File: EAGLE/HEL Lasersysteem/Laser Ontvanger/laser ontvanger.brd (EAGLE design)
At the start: 23 x 10 mm, 13 parts, among them IC1 HS0038A2, IC2 74LVC1G14DBV, IC3 74LVC1G14DBV

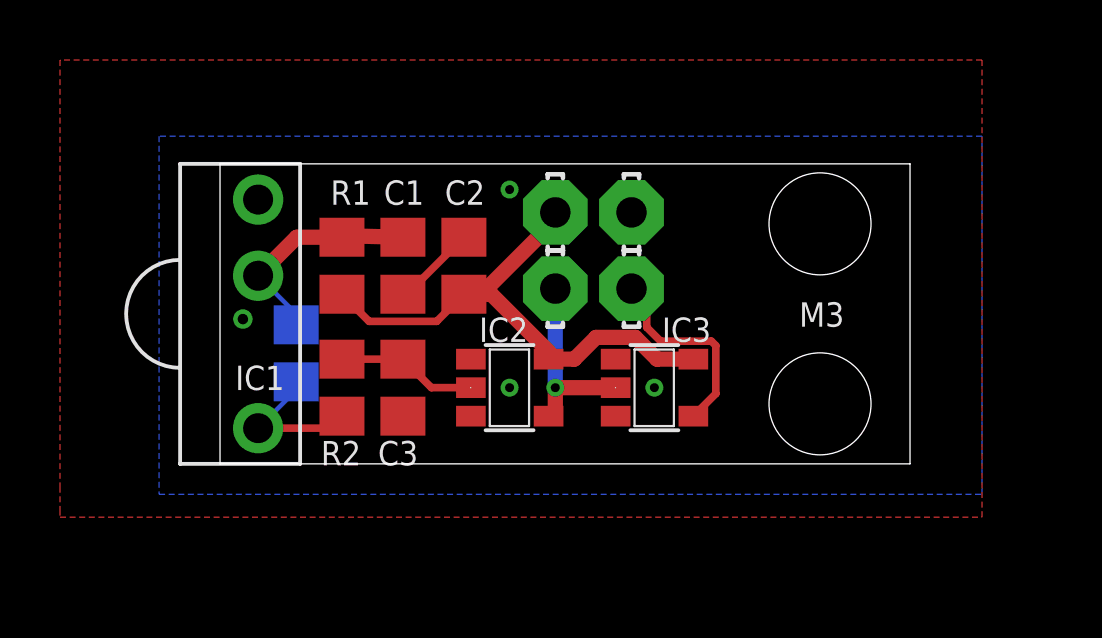
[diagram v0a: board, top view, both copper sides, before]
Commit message: Laser PCB's aangepast
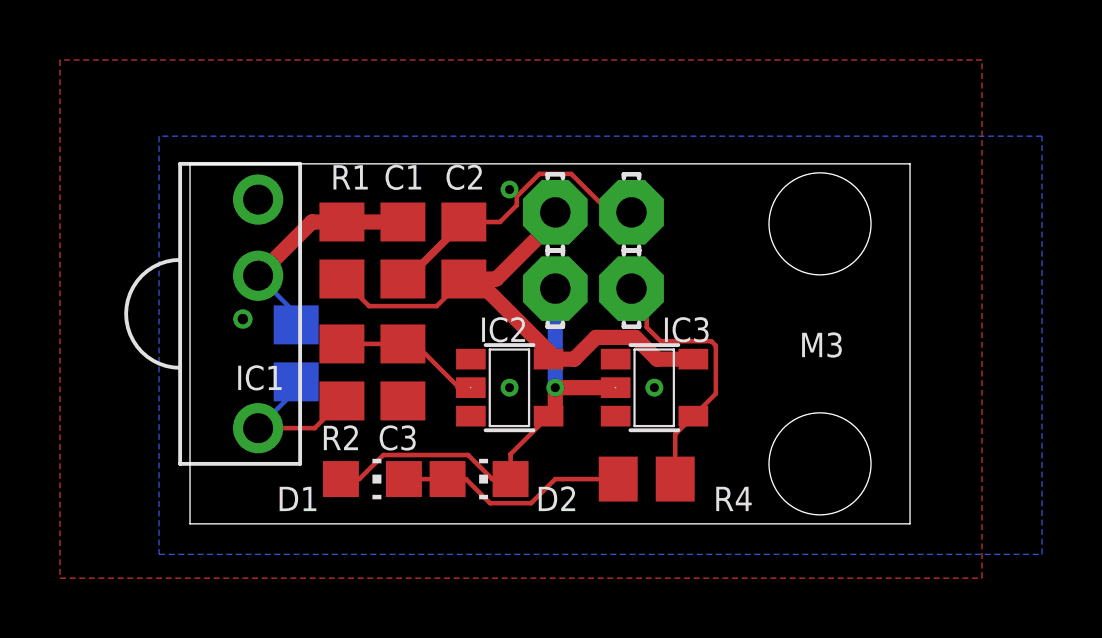
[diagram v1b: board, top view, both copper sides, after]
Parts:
- added D1: GREEN, led:CHIP-LED0805
- added D2: RED, led:CHIP-LED0805
- added R4: 1k, rcl:R0805
- moved C1 0.51 mm to (6.10, 7.11)
- moved C2 0.51 mm to (8.13, 7.11)
- moved C3 0.51 mm to (6.10, 3.05)
- moved R1 0.51 mm to (4.06, 7.11)
- moved R2 0.51 mm to (4.06, 3.05)
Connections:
- new net N$2: D1.C, D2.A, R4.1
- net N$3: now also D1.A, D2.C
- net N$4: now also R4.2
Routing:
- net N$3: track 6.36 -> 15.3 mm
- net N$2: track 0.00 -> 7.81 mm
- net GND: track 2.82 -> 9.77 mm
- net N$4: track 6.72 -> 9.07 mm
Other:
- board size 23 x 10 mm -> 24 x 12 mm

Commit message: tweede versie laser gerbers klaargemaakt voor bestelling
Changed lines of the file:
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@@
 <hole x="20" y="8" drill="3.4"/>
 <text x="19.304" y="3.556" size="0.8128" layer="21">M3</text>
-<text x="4.191" y="-1.524" size="0.8128" layer="26" rot="MR90">HEL Laserontv.
+<text x="3.556" y="-1.524" size="0.8128" layer="26" rot="MR90">HEL Laserontv.
 Kaya Hartwig
 (c) 2019</text>
@@
 </element>
 <element name="GND" library="solpad" library_urn="urn:adsk.eagle:library:364" package="LSP10" package3d_urn="urn:adsk.eagle:package:26501/1" value="LSP10" x="13.716" y="8.382" smashed="yes" rot="R270">
-<attribute name="NAME" x="14.986" y="8.636" size="0.8128" layer="26" ratio="10" rot="MR180"/>
+<attribute name="NAME" x="15.24" y="7.112" size="0.8128" layer="26" ratio="10" rot="MR90"/>
 <attribute name="VALUE" x="13.97" y="8.382" size="0.0254" layer="27" rot="R270"/>
 </element>
@@
 </element>
 <element name="VCC" library="solpad" library_urn="urn:adsk.eagle:library:364" package="LSP10" package3d_urn="urn:adsk.eagle:package:26501/1" value="LSP10" x="11.176" y="8.382" smashed="yes" rot="R270">
-<attribute name="NAME" x="7.366" y="8.636" size="0.8128" layer="26" ratio="10" rot="MR180"/>
+<attribute name="NAME" x="8.636" y="7.112" size="0.8128" layer="26" ratio="10" rot="MR90"/>
 <attribute name="VALUE" x="11.43" y="8.382" size="0.0254" layer="27" rot="R270"/>
 </element>
@@
 </element>
 <element name="OUT+" library="solpad" library_urn="urn:adsk.eagle:library:364" package="LSP10" package3d_urn="urn:adsk.eagle:package:26501/1" value="LSP10" x="13.716" y="5.842" smashed="yes" rot="R270">
-<attribute name="NAME" x="12.954" y="4.572" size="0.8128" layer="26" ratio="10" rot="MR180"/>
+<attribute name="NAME" x="15.24" y="4.064" size="0.8128" layer="26" ratio="10" rot="MR90"/>
 <attribute name="VALUE" x="13.97" y="5.842" size="0.0254" layer="27" rot="R270"/>
 </element>
 <element name="OUT-" library="solpad" library_urn="urn:adsk.eagle:library:364" package="LSP10" package3d_urn="urn:adsk.eagle:package:26501/1" value="LSP10" x="11.176" y="5.842" smashed="yes" rot="R270">
-<attribute name="NAME" x="10.16" y="4.572" size="0.8128" layer="26" ratio="10" rot="MR180"/>
+<attribute name="NAME" x="8.636" y="4.572" size="0.8128" layer="26" ratio="10" rot="MR90"/>
 <attribute name="VALUE" x="11.43" y="5.842" size="0.0254" layer="27" rot="R270"/>
 </element>
@@
 <contactref element="C3" pad="2"/>
 <polygon width="0.1524" layer="1">
-<vertex x="25.4" y="-3.81"/>
-<vertex x="25.4" y="13.462"/>
+<vertex x="17.272" y="-3.81"/>
+<vertex x="17.272" y="13.462"/>
 <vertex x="-5.334" y="13.462"/>
 <vertex x="-5.334" y="-3.81"/>
@@
 <vertex x="-2.032" y="10.922"/>
 <vertex x="-2.032" y="-3.016"/>
-<vertex x="27.4" y="-3.016"/>
-<vertex x="27.4" y="10.922"/>
+<vertex x="17.24" y="-3.016"/>
+<vertex x="17.24" y="10.922"/>
 </polygon>
 <via x="9.652" y="2.54" extent="1-16" drill="0.3"/>
